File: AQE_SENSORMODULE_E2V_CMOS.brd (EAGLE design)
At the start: 31.2 x 39.9 mm, 33 parts, among them J1 440055-4, J2 AVR_SPI_PRG_6NS, U1 V_REG_LDOSMD, U2 V_REG_LDOSMD

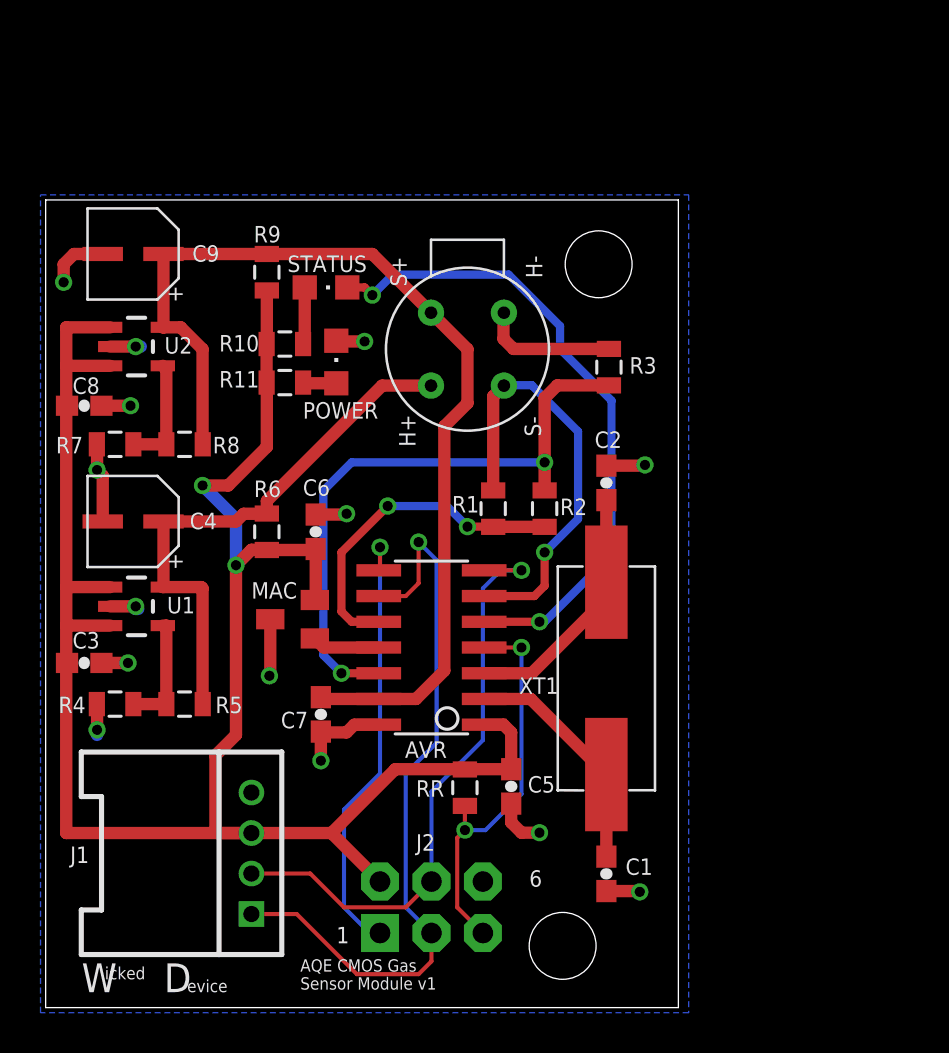
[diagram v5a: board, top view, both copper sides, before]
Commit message: making progress on updates to incorporate heater feedback control
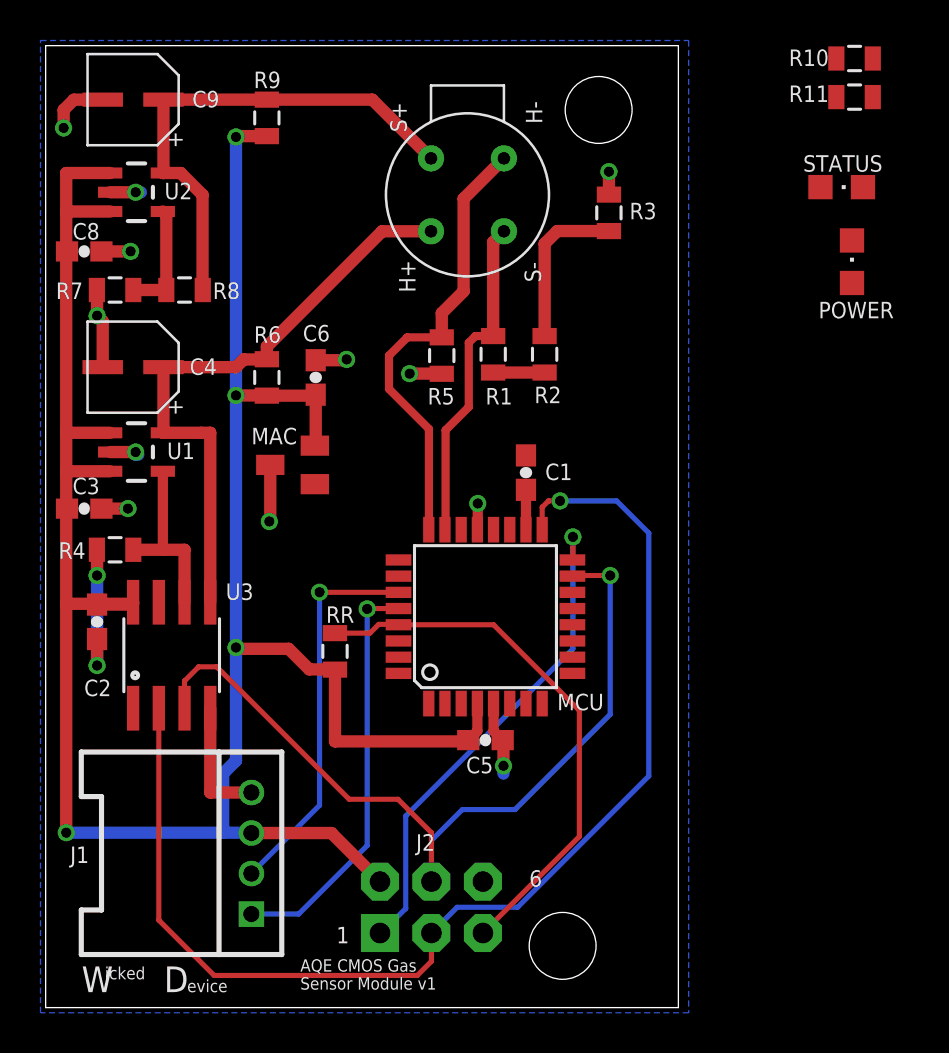
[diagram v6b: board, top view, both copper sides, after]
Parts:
- removed AVR: TINY24/44/84-SSU, avr-7:SOIC14
- removed C7: 0.1uF, SparkFun:0603-CAP
- removed XT1: ABLS, wicked-device:ABLS
- added MCU: ATTINY4832A, axeio-SparkFun:TQFP32-08
- added U3: MCP41XXX, SparkFun-AnalogIC:SO08
- C1, C2: value 22pF -> 0.1uF
- R5: value 2.2MOhm -> (none)
- moved R10 31.5 mm to (39.9, 46.9)
- moved R11 31.5 mm to (39.9, 45.0)
- moved C2 26.1 mm to (2.54, 19.1), turned to 270 degrees
- moved POWER 25.9 mm to (39.8, 36.8)
- moved STATUS 25.9 mm to (39.3, 40.5)
- moved R5 21.4 mm to (19.6, 32.2), turned to 90 degrees
- moved C1 20.2 mm to (23.7, 26.4), turned to 90 degrees
- moved RR 9.30 mm to (14.3, 17.6), turned to 270 degrees
- moved C9 7.62 mm to (4.32, 44.8)
- moved C3 7.62 mm to (1.91, 24.6)
- moved C4 7.62 mm to (4.32, 31.6)
- moved C8 7.62 mm to (1.91, 37.3)
- moved MAC 7.62 mm to (12.2, 26.8)
- moved R1 7.62 mm to (22.1, 32.3)
- moved R2 7.62 mm to (24.6, 32.3)
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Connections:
- removed net N$1: R4.2, R5.1, U1.4
- removed net XTAL1: AVR.3, C2.1, XT1.2
- removed net XTAL2: AVR.2, C1.1, XT1.1
- new net /POT_CS: U3.1
- new net AGND: C1.2
- new net AVCC: C1.1, MCU.18
- new net HEATER_FEEDBACK: MCU.24, R5.2, U$4.FIGV+/E2V-
- new net MOSI: J2.4, MCU.15, U3.3
- new net N$10: MCU.13
- new net N$11: MCU.14
- new net N$15: MCU.7
- new net N$16: MCU.8
- new net N$19: MCU.25
- new net N$20: MCU.26
- new net N$23: MCU.20
- new net N$24: MCU.30
- new net N$25: MCU.31
- new net N$26: MCU.32
- new net N$27: MCU.1
- new net N$28: MCU.2
- new net N$29: MCU.9
- new net N$30: MCU.10
- new net N$31: MCU.11
- new net N$5: MCU.19
- new net N$6: MCU.22
- new net N$7: MCU.3
- new net N$8: MCU.6
- new net N$9: MCU.12
- new net POWER: POWER.C
- new net RH-: R4.2, U1.4, U3.6
- new net SCK: J2.3, MCU.17, U3.2
- net /R1_SEL: no longer AVR.10
- net /R2_SEL: no longer AVR.12
- net /RESET: now also MCU.29; no longer AVR.4
- net GND: now also MCU.21, MCU.5, R5.1, U3.4; no longer AVR.14, C1.2, C7.2, POWER.C, U$4.FIGV+/E2V-
- net HEATER_VCC: now also U3.5; no longer R5.2
- net MAC_IO: no longer AVR.11
- net MISO: now also MCU.16; no longer AVR.8
- net SCL: now also MCU.28; no longer AVR.9, J2.3
- net SDA: now also MCU.27; no longer AVR.7, J2.4
- net SENSOR: now also MCU.23; no longer AVR.6
- net SENSOR_VCC: no longer AVR.13, C7.1
- net STATUS: no longer AVR.5
- net VCC: now also C2.1, MCU.4, U3.8; no longer AVR.1
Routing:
- net SCK: track 0.00 -> 59.8 mm, vias 0 -> 1
- net MOSI: track 0.00 -> 41.8 mm, vias 0 -> 1
- net STATUS: track 32.1 -> 0.00 mm, vias 2 -> 0
- net SENSOR_VCC: track 50.8 -> 25.2 mm
- net /R2_SEL: track 30.7 -> 7.99 mm, vias 2 -> 0
- net HEATER_FEEDBACK: track 0.00 -> 22.5 mm
- net VCC: track 102.6 -> 123.4 mm, vias 2 -> 4
- net SCL: track 36.9 -> 20.4 mm
- net /R1_SEL: track 16.4 -> 2.54 mm, vias 2 -> 0
- net XTAL1: track 12.6 -> 0.00 mm
- net XTAL2: track 11.6 -> 0.00 mm
- net SDA: track 29.8 -> 19.2 mm
- net RH-: track 0.00 -> 9.10 mm
- net /RESET: track 19.8 -> 27.0 mm, vias 2 -> 0
- net N$1: track 5.73 -> 0.00 mm
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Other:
- board size 31.2 x 39.9 mm -> 31.2 x 47.5 mm

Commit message: routed additional signals, would like to separate analog ground plane
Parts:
- removed POWER: RED, adafruit:CHIPLED_0805
- removed STATUS: GREEN, adafruit:CHIPLED_0805
- added INFO: GREEN, adafruit:CHIPLED_0805
- added PWR: RED, adafruit:CHIPLED_0805
- moved R10 21.7 mm to (29.6, 27.7), turned to 270 degrees
- moved R11 21.3 mm to (27.4, 27.7), turned to 270 degrees
- moved JP1 1.91 mm to (27.3, 3.75)
- moved C1 0.38 mm to (23.7, 26.8)
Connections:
- removed net N$10: MCU.13
- removed net N$11: MCU.14
- removed net N$15: MCU.7
- removed net N$16: MCU.8
- removed net N$19: MCU.25
- removed net N$20: MCU.26
- removed net N$23: MCU.20
- removed net N$24: MCU.30
- removed net N$25: MCU.31
- removed net N$26: MCU.32
- removed net N$27: MCU.1
- removed net N$28: MCU.2
- removed net N$29: MCU.9
- removed net N$30: MCU.10
- removed net N$31: MCU.11
- removed net N$5: MCU.19
- removed net N$6: MCU.22
- removed net N$7: MCU.3
- removed net N$8: MCU.6
- removed net N$9: MCU.12
- net /R1_SEL: now also MCU.20
- net /R2_SEL: now also MCU.19
- net GND: now also INFO.C, PWR.C
- net MAC_IO: now also MCU.25
- net N$3: now also PWR.A; no longer POWER.A
- net N$4: now also INFO.A; no longer STATUS.A
- net POWER: now also MCU.14, R11.2; no longer POWER.C
- net STATUS: now also MCU.13, R10.2; no longer STATUS.C
- net VCC: no longer R10.2, R11.2
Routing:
- net /R2_SEL: track 7.99 -> 21.3 mm
- net STATUS: track 0.00 -> 10.5 mm
- net POWER: track 0.00 -> 9.81 mm
- net /R1_SEL: track 2.54 -> 10.3 mm
- net MAC_IO: track 0.00 -> 6.37 mm
- net GND: track 39.5 -> 42.9 mm, vias 14 -> 16
- net N$4: track 0.00 -> 2.81 mm
- net N$3: track 0.00 -> 2.81 mm

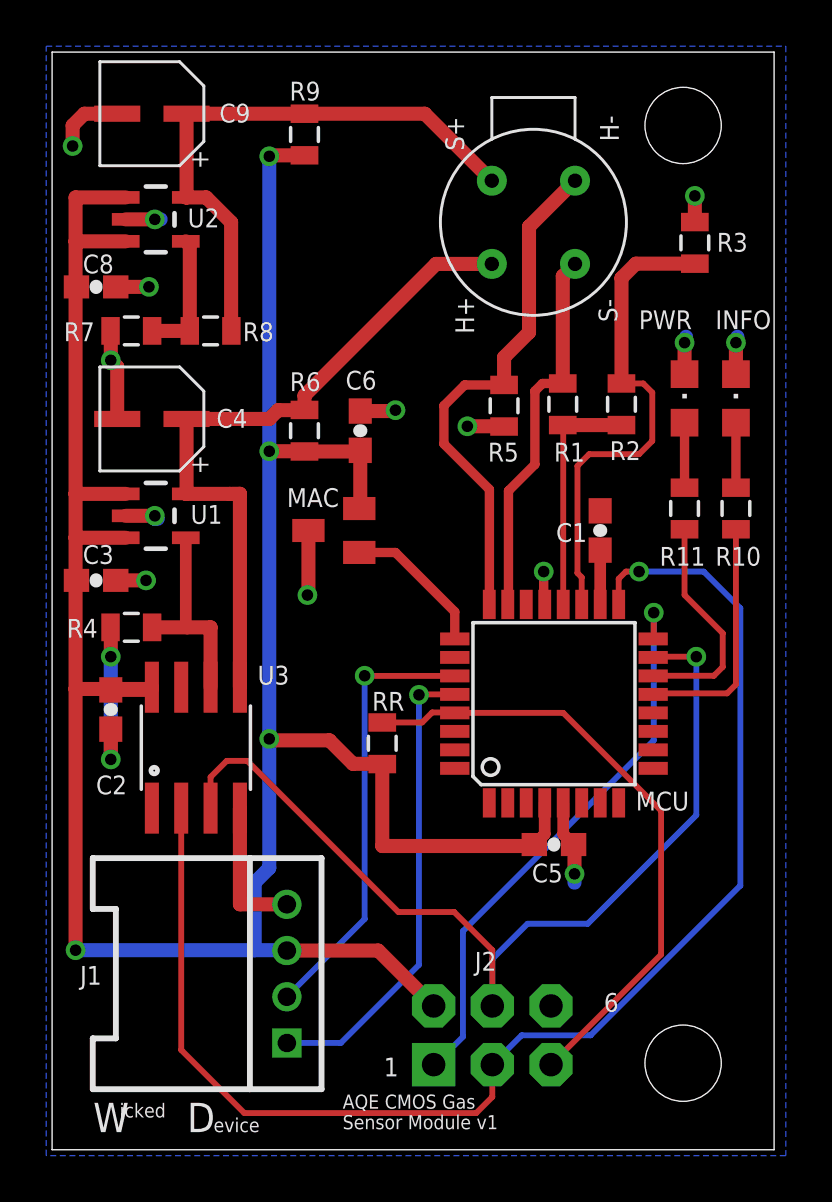
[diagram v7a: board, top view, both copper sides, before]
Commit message: incorporated changes for separating analog and digital gnd with a star topology. added possibility to shut off heater power, and added power filtering for analog vcc to mcu
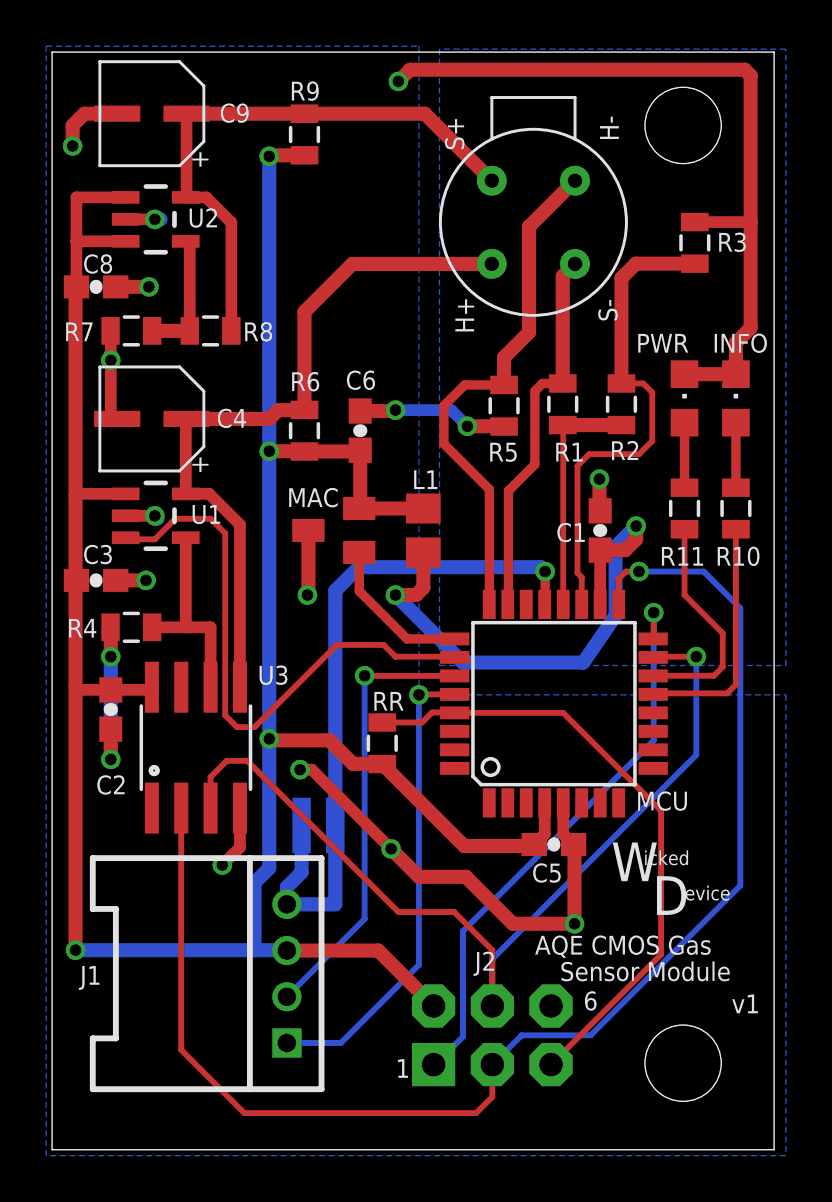
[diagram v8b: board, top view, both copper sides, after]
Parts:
- added L1: FERRITE, nanodeRF_11:RCL_R0805
- added U$2, U$3: PLANE_COUPLER, wicked-device:PLANE_COUPLER
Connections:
- new net HEATER_EN: MCU.26, U1.3
- new net RETURN_GND: J1.4, U$2.2, U$3.2
- net AGND: now also MCU.21, U$2.1
- net AVCC: now also L1.1
- net GND: now also U$3.1; no longer J1.4, MCU.21
- net VCC: now also L1.2; no longer U1.3
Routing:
- net GND: track 42.9 -> 87.2 mm
- net HEATER_EN: track 0.00 -> 24.7 mm
- net AGND: track 0.00 -> 22.3 mm, vias 0 -> 2
- net AVCC: track 2.35 -> 23.7 mm, vias 0 -> 2
- net RETURN_GND: track 0.00 -> 7.99 mm
- net VCC: track 123.4 -> 120.3 mm
- net MOSI: track 41.8 -> 40.3 mm
- net HEATER_VCC: track 30.3 -> 31.7 mm
- added copper zone on layer 16, net AGND
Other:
- board text added: "Sensor Module"
- board text added: "v1"
- board text removed: "Sensor Module v1"
